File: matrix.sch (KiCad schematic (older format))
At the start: 142 parts, among them SW1.1 Backtick, SW1.10 9, SW1.11 0, SW1.12 -, SW1.13 =, SW1.2 1, SW1.3 2, SW1.4 3, SW1.5 4, SW1.6 5, SW1.7 6, SW1.8 7, SW1.9 8, SW2.1 Tab, SW2.10 I, SW2.11 O, SW2.12 P, SW2.13 /, SW2.2 Q, SW2.3 W, SW2.4 E, SW2.5 R, SW2.6 T, SW2.8 Y, SW2.9 U, SW3.1 Bksp, SW3.10 K, SW3.11 L, SW3.12 ;, SW3.13 Enter, SW3.2 A, SW3.3 S, SW3.4 D, SW3.5 F, SW3.6 G, SW3.7 B, SW3.8 H, SW3.9 J, SW4.7 Fn, SW4A1 LShift, SW4A10 ,, SW4A11 ., SW4A13 RShift, SW4A3 Z, SW4A4 X, SW4A5 C, SW4A6 V, SW4A8 N, SW4A9 M, SW4B1 LShift, SW4B10 ,, SW4B11 ., SW4B12 ., SW4B13 RShift, SW4B2 Z, SW4B3 Z, SW4B4 X, SW4B5 C, SW4B6 V, SW4B8 N, SW4B9 M, SW4C1 LShift, SW4C12 ., SW4C13 RShift, SW4C2 Z, SW5A1 LCtrl, SW5A10 1.5, SW5A12 1.5, SW5A13 1.5, SW5A2 LGUI, SW5A4 LAlt, SW5A7 Space, SW5B1 LCtrl, SW5B10 1.25, SW5B12 1.25, SW5B13 1.25, SW5B2 LGUI, SW5B4 LAlt, SW5B7 Space, SW5C10 1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

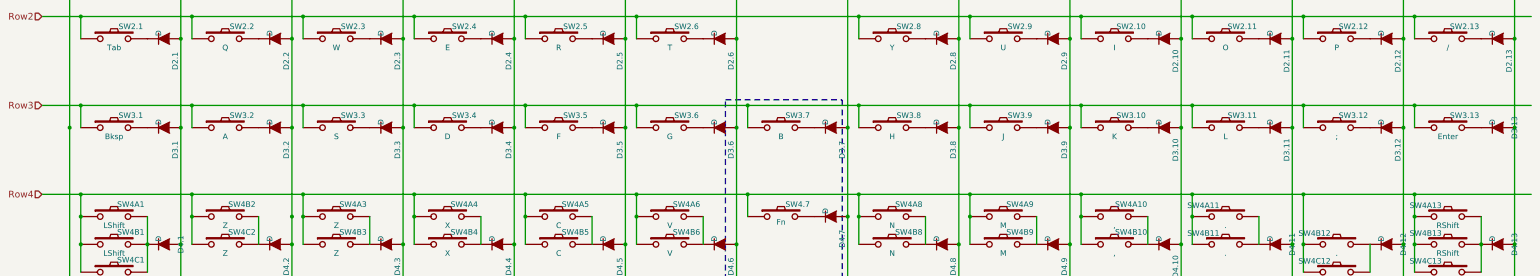
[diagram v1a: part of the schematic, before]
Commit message: Begun work for rev 1 layout, which supports ortholinear rows 2 and 3.
Converted all switches to use platemount footprint.  Added additional
set of switches to row 3 for a completely ortholinear layout.
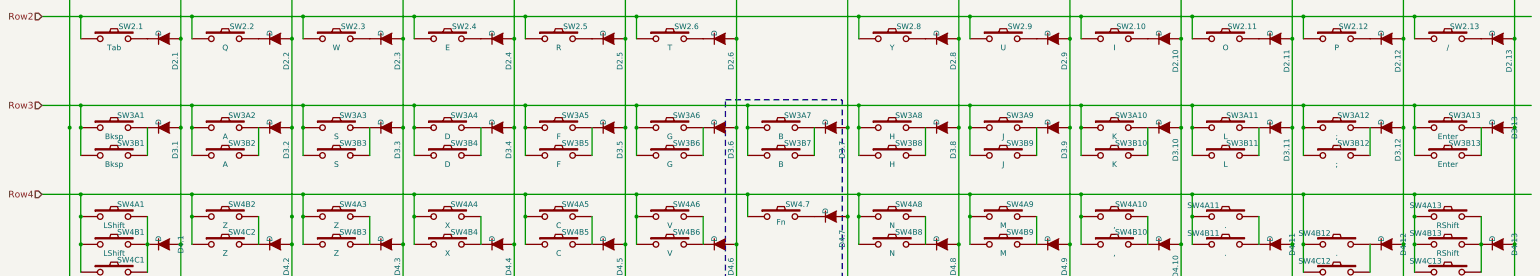
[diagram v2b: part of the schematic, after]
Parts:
- added SW3B1: Bksp, footprints:MX_100_Plate, symbol SW_PUSH
- added SW3B10: K, footprints:MX_100_Plate, symbol SW_PUSH
- added SW3B11: L, footprints:MX_100_Plate, symbol SW_PUSH
- added SW3B12: ;, footprints:MX_100_Plate, symbol SW_PUSH
- added SW3B13: Enter, footprints:MX_100_Plate, symbol SW_PUSH
- added SW3B2: A, footprints:MX_100_Plate, symbol SW_PUSH
- added SW3B3: S, footprints:MX_100_Plate, symbol SW_PUSH
- added SW3B4: D, footprints:MX_100_Plate, symbol SW_PUSH
- added SW3B5: F, footprints:MX_100_Plate, symbol SW_PUSH
- added SW3B6: G, footprints:MX_100_Plate, symbol SW_PUSH
- added SW3B7: B, footprints:MX_100_Plate, symbol SW_PUSH
- added SW3B8: H, footprints:MX_100_Plate, symbol SW_PUSH
- added SW3B9: J, footprints:MX_100_Plate, symbol SW_PUSH
- SW1.1, SW1.10, SW1.11, SW1.12, SW1.13, SW1.2, SW1.3, SW1.4, SW1.5, SW1.6, SW1.7, SW1.8, SW1.9, SW2.10, SW2.11, SW2.12, SW2.2, SW2.3, SW2.4, SW2.5, SW2.6, SW2.8, SW2.9, SW4A10, SW4A11, SW4A3, SW4A4, SW4A5, SW4A6, SW4A8, SW4A9, SW4B10, SW4B11, SW4B12, SW4B2, SW4B3, SW4B4, SW4B5, SW4B6, SW4B8, SW4B9, SW4C1, SW4C12, SW4C13, SW4C2, SW5A12, SW5A2, SW5C10, SW5C11, SW5C12, SW5C13: footprint Keyboards:CHERRY_PCB_100H_NoBound -> footprints:MX_100_Plate
- SW2.1, SW2.13, SW4B1, SW5A1, SW5A10, SW5A13, SW5A4: footprint Keyboards:CHERRY_PCB_150H_NoBound -> footprints:MX_150_Plate
- SW3A1: renamed from SW3.1; footprint Keyboards:CHERRY_PCB_150H_NoBound -> footprints:MX_150_Plate
- SW3A10: renamed from SW3.10; footprint Keyboards:CHERRY_PCB_100H_NoBound -> footprints:MX_100_Plate
- SW3A11: renamed from SW3.11; footprint Keyboards:CHERRY_PCB_100H_NoBound -> footprints:MX_100_Plate
- SW3A12: renamed from SW3.12; footprint Keyboards:CHERRY_PCB_100H_NoBound -> footprints:MX_100_Plate
- SW3A13: renamed from SW3.13; footprint Keyboards:CHERRY_PCB_150H_NoBound -> footprints:MX_150_Plate
- SW3A2: renamed from SW3.2; footprint Keyboards:CHERRY_PCB_100H_NoBound -> footprints:MX_100_Plate
- SW3A3: renamed from SW3.3; footprint Keyboards:CHERRY_PCB_100H_NoBound -> footprints:MX_100_Plate
- SW3A4: renamed from SW3.4; footprint Keyboards:CHERRY_PCB_100H_NoBound -> footprints:MX_100_Plate
- SW3A5: renamed from SW3.5; footprint Keyboards:CHERRY_PCB_100H_NoBound -> footprints:MX_100_Plate
- SW3A6: renamed from SW3.6; footprint Keyboards:CHERRY_PCB_100H_NoBound -> footprints:MX_100_Plate
- SW3A7: renamed from SW3.7; footprint Keyboards:CHERRY_PCB_100H_NoBound -> footprints:MX_100_Plate
- SW3A8: renamed from SW3.8; footprint Keyboards:CHERRY_PCB_100H_NoBound -> footprints:MX_100_Plate
- SW3A9: renamed from SW3.9; footprint Keyboards:CHERRY_PCB_100H_NoBound -> footprints:MX_100_Plate
- SW4.7: footprint Keyboards:CHERRY_PCB_225H_NoBound -> footprints:MX_225_Plate
- SW4A1, SW4A13: footprint Keyboards:CHERRY_PCB_200H_NoBound -> footprints:MX_200_Plate
- SW4B13: footprint Keyboards:CHERRY_PCB_100H_NoBound -> footprints:MX_150_Plate
- SW5A7, SW5B7: footprint Keyboards:CHERRY_PCB_275H_NoBound -> footprints:MX_275_Plate
- SW5B1, SW5B10, SW5B12, SW5B13, SW5B2, SW5B4: footprint Keyboards:CHERRY_PCB_125H_NoBound -> footprints:MX_125_Plate
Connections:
- wire segments 97 -> 110

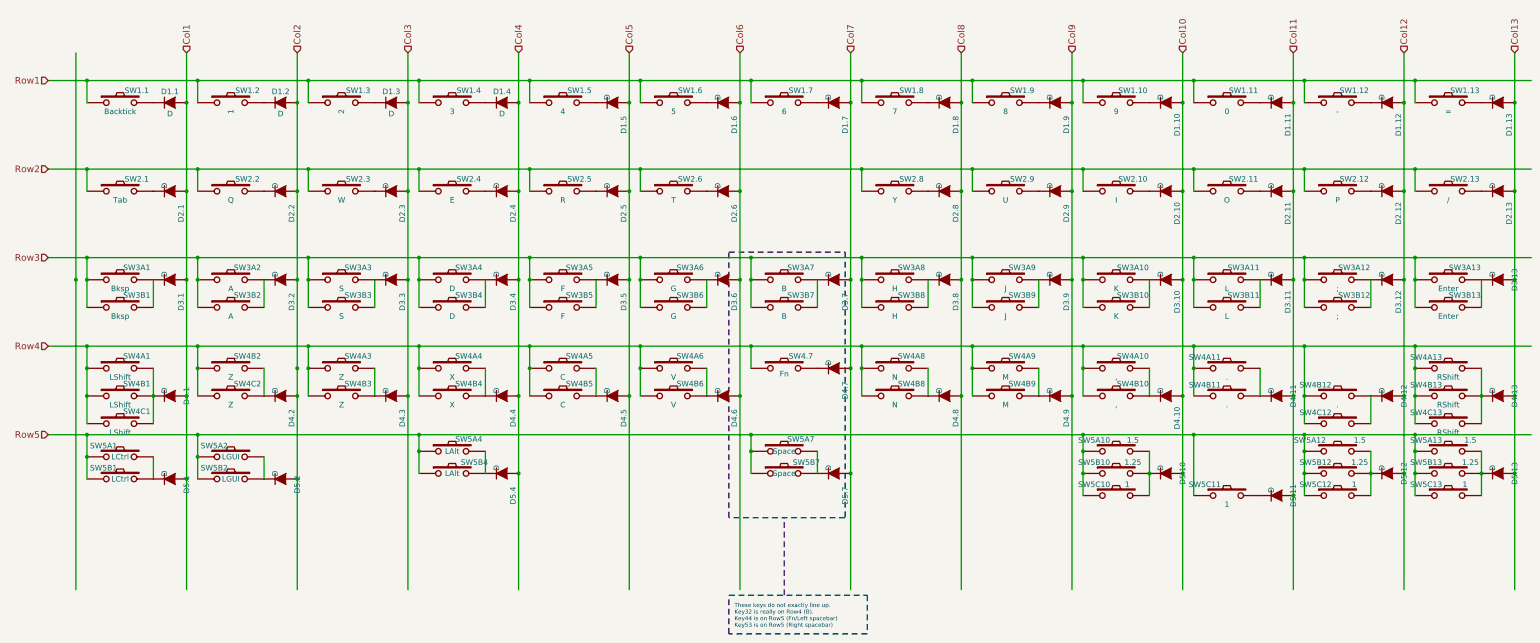
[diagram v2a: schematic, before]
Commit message: Ortholinear switch footprints added to row 2.
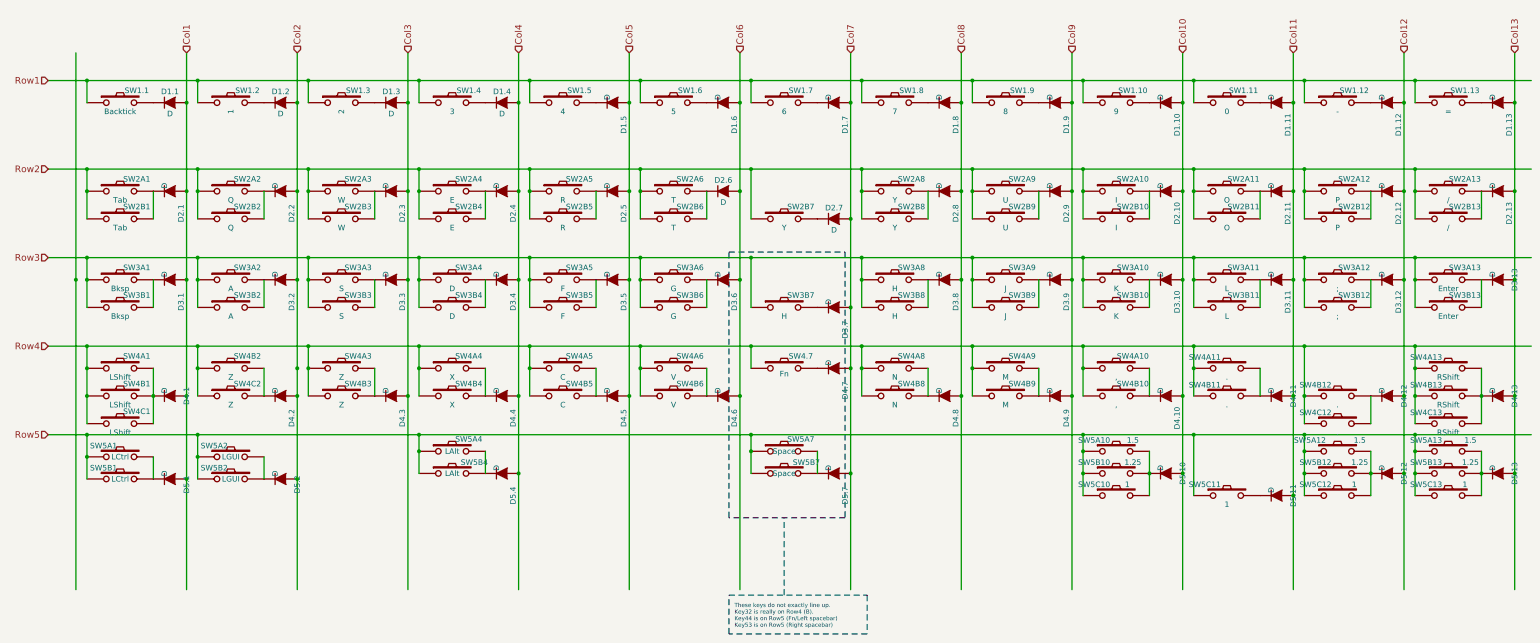
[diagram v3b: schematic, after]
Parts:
- removed SW3A7: B, footprints:MX_100_Plate, symbol SW_PUSH
- added D2.7: D, Diodes_SMD:D_SOD-323_HandSoldering, symbol D
- added SW2B1: Tab, footprints:MX_100_Plate, symbol SW_PUSH
- added SW2B10: I, footprints:MX_100_Plate, symbol SW_PUSH
- added SW2B11: O, footprints:MX_100_Plate, symbol SW_PUSH
- added SW2B12: P, footprints:MX_100_Plate, symbol SW_PUSH
- added SW2B13: /, footprints:MX_100_Plate, symbol SW_PUSH
- added SW2B2: Q, footprints:MX_100_Plate, symbol SW_PUSH
- added SW2B3: W, footprints:MX_100_Plate, symbol SW_PUSH
- added SW2B4: E, footprints:MX_100_Plate, symbol SW_PUSH
- added SW2B5: R, footprints:MX_100_Plate, symbol SW_PUSH
- added SW2B6: T, footprints:MX_100_Plate, symbol SW_PUSH
- added SW2B7, SW2B8: Y, footprints:MX_100_Plate, symbol SW_PUSH
- added SW2B9: U, footprints:MX_100_Plate, symbol SW_PUSH
- SW3B7: value B -> H
- renumbered SW2.1 to SW2A1, SW2.10 to SW2A10, SW2.11 to SW2A11, SW2.12 to SW2A12, SW2.13 to SW2A13, SW2.2 to SW2A2, SW2.3 to SW2A3, SW2.4 to SW2A4, SW2.5 to SW2A5, SW2.6 to SW2A6, SW2.8 to SW2A8, SW2.9 to SW2A9
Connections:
- wire segments 110 -> 122
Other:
- moved on the sheet: D3.7

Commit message: Added a bunch of additional switches for layouts
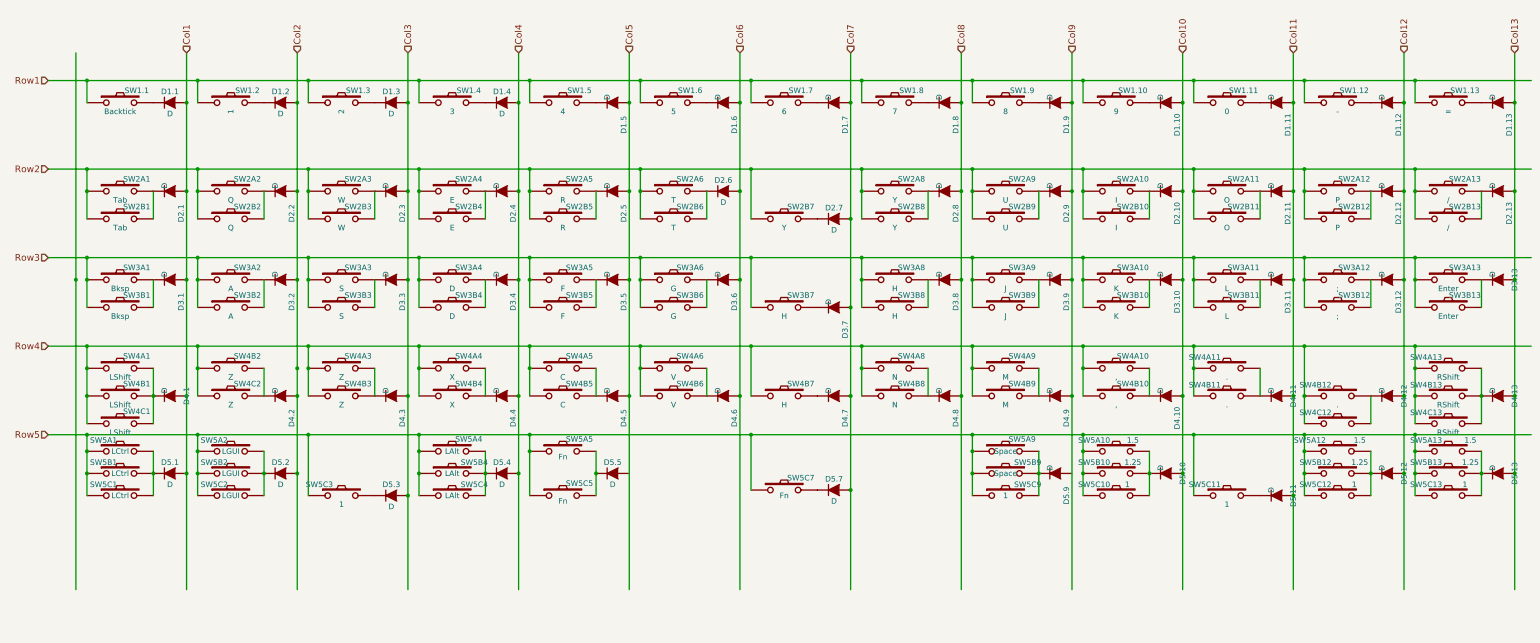
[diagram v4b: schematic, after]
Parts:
- added D5.3, D5.5, D5.7: D, Diodes_SMD:D_SOD-323_HandSoldering, symbol D
- added SW4B7: H, footprints:MX_100_Plate, symbol SW_PUSH
- added SW5C1: LCtrl, footprints:MX_100_Plate, symbol SW_PUSH
- added SW5C2: LGUI, footprints:MX_100_Plate, symbol SW_PUSH
- added SW5C3, SW5C9: 1, footprints:MX_100_Plate, symbol SW_PUSH
- added SW5C4: LAlt, footprints:MX_100_Plate, symbol SW_PUSH
- added SW5C5, SW5C7: Fn, footprints:MX_200_Plate, symbol SW_PUSH
- renumbered SW4.7 to SW5A5, SW5A7 to SW5A9, SW5B7 to SW5B9
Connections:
- wire segments 122 -> 126
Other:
- note removed: "These keys do not exactly line up.\nKey32 is really on Row4 (B).\nKey44 is on Row5 (Fn/Left spacebar)\nKey53 is on Row5 (Right spacebar)"
- moved on the sheet: D4.7, D5.1, D5.2, D5.9, SW5A1, SW5A2, SW5A5, SW5A9, SW5B1, SW5B2, SW5B9

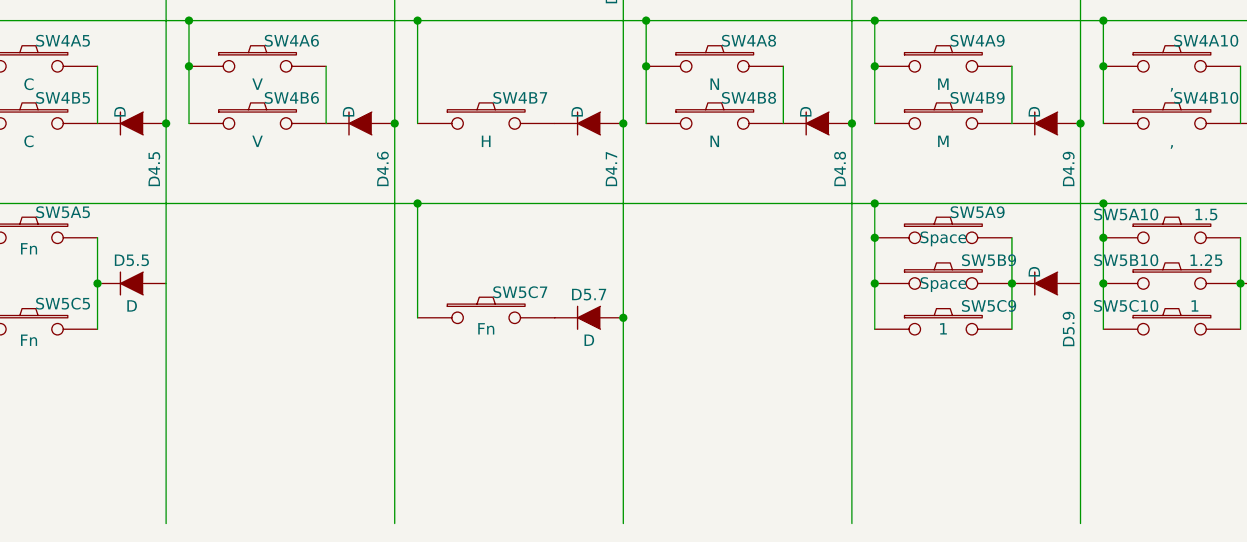
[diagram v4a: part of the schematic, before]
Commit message: All switch columns wired.
Wired all switches in a column together and dropped the 10 existing
WS2812Bs in place.  Need to connect everything to controller.
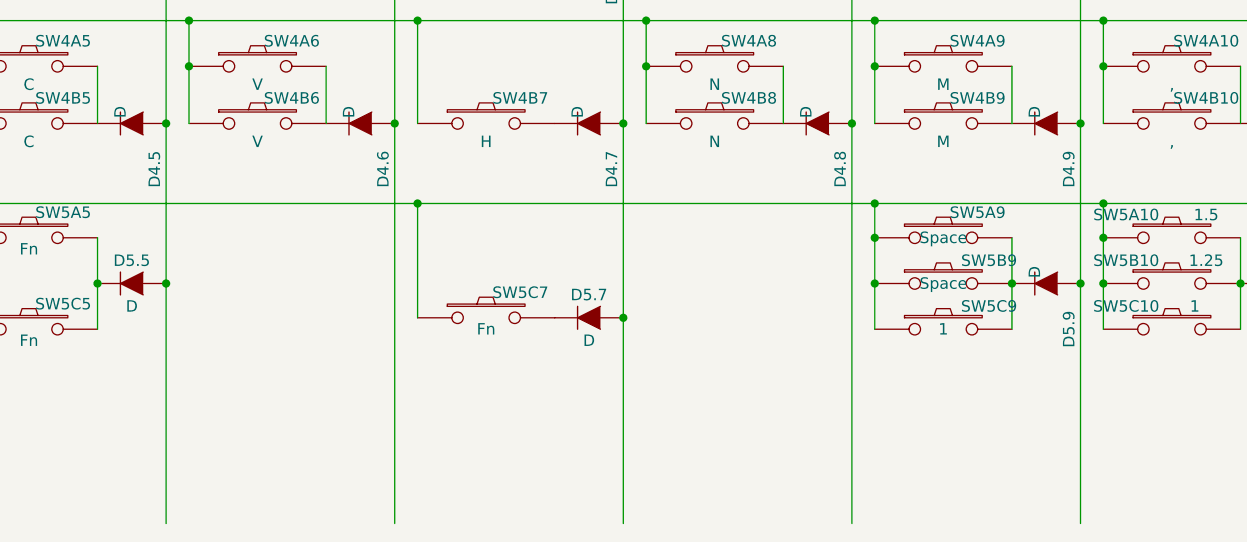
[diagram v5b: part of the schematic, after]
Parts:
- SW4A1, SW4A13, SW5C5, SW5C7: footprint footprints:MX_200_Plate -> footprints:MX_200_Plate_NoStabHoles
- SW5A5: footprint footprints:MX_225_Plate -> footprints:MX_225_Plate_NoStabHoles
- SW5A9, SW5B9: footprint footprints:MX_275_Plate -> footprints:MX_275_Plate_NoStabHoles
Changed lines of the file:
@@
 F 0 "SW4A1" H 2850 4610 50  0000 C CNN
 F 1 "LShift" H 2700 4420 50  0000 C CNN
-F 2 "footprints:MX_200_Plate" H 2700 4500 50  0001 C CNN
+F 2 "footprints:MX_200_Plate_NoStabHoles" H 2700 4500 50  0001 C CNN
 F 3 "" H 2700 4500 50  0000 C CNN
 	1    2700 4500
@@
 F 0 "SW5A5" H 6850 5360 50  0000 C CNN
 F 1 "Fn" H 6700 5200 50  0000 C CNN
-F 2 "footprints:MX_225_Plate" H 6700 5250 50  0001 C CNN
+F 2 "footprints:MX_225_Plate_NoStabHoles" H 6700 5250 50  0001 C CNN
 F 3 "" H 6700 5250 50  0000 C CNN
 	1    6700 5250
@@
 F 0 "SW4A13" H 14500 4600 50  0000 C CNN
 F 1 "RShift" H 14700 4420 50  0000 C CNN
-F 2 "footprints:MX_200_Plate" H 14700 4500 50  0001 C CNN
+F 2 "footprints:MX_200_Plate_NoStabHoles" H 14700 4500 50  0001 C CNN
 F 3 "" H 14700 4500 50  0000 C CNN
 	1    14700 4500
@@
 F 0 "SW5A9" H 10850 5360 50  0000 C CNN
 F 1 "Space" H 10700 5250 50  0000 C CNN
-F 2 "footprints:MX_275_Plate" H 10700 5250 50  0001 C CNN
+F 2 "footprints:MX_275_Plate_NoStabHoles" H 10700 5250 50  0001 C CNN
 F 3 "" H 10700 5250 50  0000 C CNN
 	1    10700 5250
@@
 F 0 "SW5B9" H 10900 5550 50  0000 C CNN
 F 1 "Space" H 10700 5450 50  0000 C CNN
-F 2 "footprints:MX_275_Plate" H 10700 5450 50  0001 C CNN
+F 2 "footprints:MX_275_Plate_NoStabHoles" H 10700 5450 50  0001 C CNN
 F 3 "" H 10700 5450 50  0000 C CNN
 	1    10700 5450
@@
 F 0 "SW5C5" H 6850 5760 50  0000 C CNN
 F 1 "Fn" H 6700 5600 50  0000 C CNN
-F 2 "footprints:MX_200_Plate" H 6700 5650 50  0001 C CNN
+F 2 "footprints:MX_200_Plate_NoStabHoles" H 6700 5650 50  0001 C CNN
 F 3 "" H 6700 5650 50  0000 C CNN
 	1    6700 5650
@@
 F 0 "SW5C7" H 8850 5710 50  0000 C CNN
 F 1 "Fn" H 8700 5550 50  0000 C CNN
-F 2 "footprints:MX_200_Plate" H 8700 5600 50  0001 C CNN
+F 2 "footprints:MX_200_Plate_NoStabHoles" H 8700 5600 50  0001 C CNN
 F 3 "" H 8700 5600 50  0000 C CNN
 	1    8700 5600
@@
 $EndComp
 Connection ~ 9300 5600
+Connection ~ 7300 5450
+Connection ~ 11300 5450
 $EndSCHEMATC
